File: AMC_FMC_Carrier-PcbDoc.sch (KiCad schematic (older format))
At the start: 17 parts

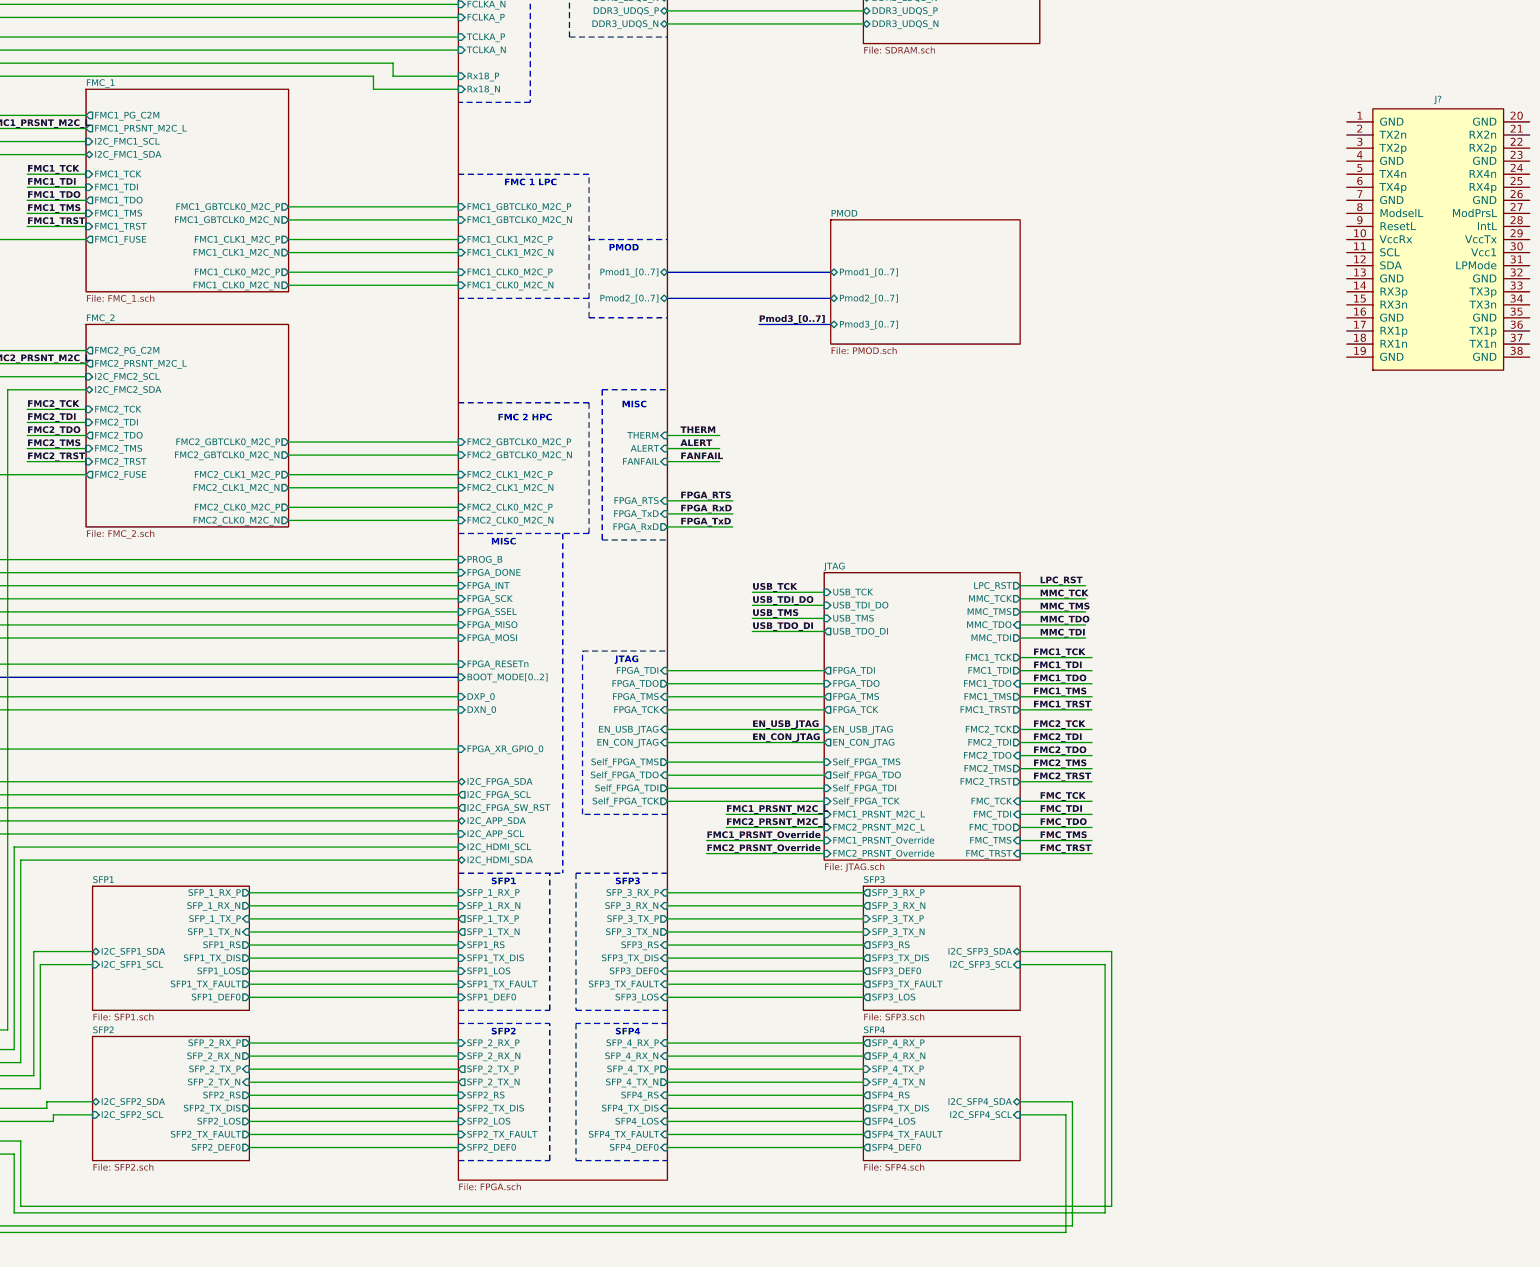
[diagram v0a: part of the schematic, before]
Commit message: MGT mux and QSFP added to the schematics,
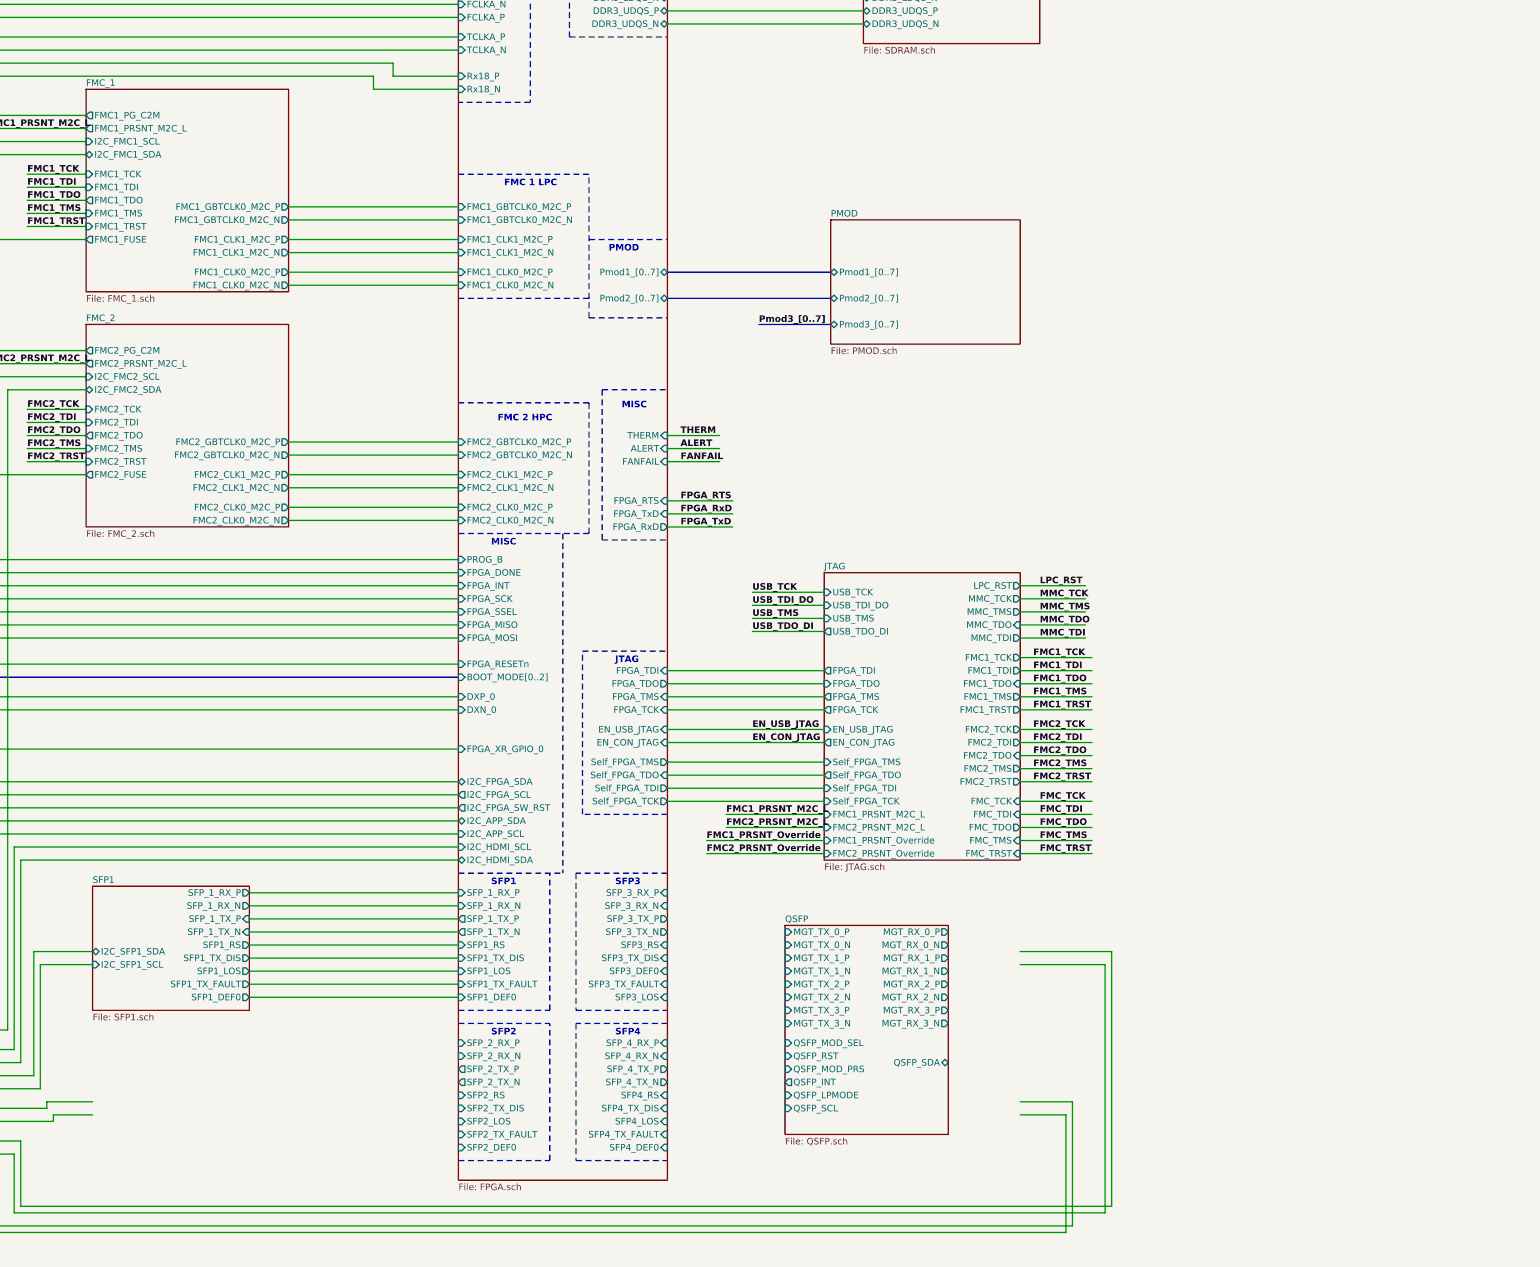
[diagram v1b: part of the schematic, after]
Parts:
- removed J?: SAMTEC_QSFP8-038-01-L-D-RA1, SAMTEC SMD:SAMTEC_QSFP8-038-01-L-D-RA1, symbol SAMTEC:SAMTEC_QSFP8-038-01-L-D-RA1
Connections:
- wire segments 364 -> 337
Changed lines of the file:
@@
 $Descr A2 23386 16535
 encoding utf-8
-Sheet 1 26
+Sheet 1 25
 Title "Marble"
 Date "2019-01-16"
@@
 Wire Wire Line
 	14450 5650 12950 5650
-$Sheet
-S 8550 13400 1200 950
-U 5CC393D3
-F0 "SFP2" 50
-F1 "SFP2.sch" 50
-F2 "SFP_2_RX_P" O R 9750 13450 50
-F3 "SFP_2_RX_N" O R 9750 13550 50
-F4 "SFP_2_TX_P" I R 9750 13650 50
-F5 "SFP_2_TX_N" I R 9750 13750 50
-F6 "I2C_SFP2_SDA" B L 8550 13900 50
-F7 "I2C_SFP2_SCL" I L 8550 14000 50
-F8 "SFP2_TX_DIS" O R 9750 13950 50
-F9 "SFP2_TX_FAULT" O R 9750 14150 50
-F10 "SFP2_DEF0" O R 9750 14250 50
-F11 "SFP2_LOS" O R 9750 14050 50
-F12 "SFP2_RS" O R 9750 13850 50
-$EndSheet
-$Sheet
-S 14450 12250 1200 950
-U 5CC6DBF7
-F0 "SFP3" 50
-F1 "SFP3.sch" 50
-F2 "SFP_3_RX_P" O L 14450 12300 50
-F3 "SFP_3_RX_N" O L 14450 12400 50
-F4 "SFP_3_TX_P" I L 14450 12500 50
-F5 "SFP_3_TX_N" I L 14450 12600 50
-F6 "I2C_SFP3_SDA" B R 15650 12750 50
-F7 "I2C_SFP3_SCL" I R 15650 12850 50
-F8 "SFP3_TX_DIS" O L 14450 12800 50
-F9 "SFP3_TX_FAULT" O L 14450 13000 50
-F10 "SFP3_DEF0" O L 14450 12900 50
-F11 "SFP3_LOS" O L 14450 13100 50
-F12 "SFP3_RS" O L 14450 12700 50
-$EndSheet
-$Sheet
-S 14450 13400 1200 950
-U 5CC8AFE1
-F0 "SFP4" 50
-F1 "SFP4.sch" 50
-F2 "SFP_4_RX_P" O L 14450 13450 50
-F3 "SFP_4_RX_N" O L 14450 13550 50
-F4 "SFP_4_TX_P" I L 14450 13650 50
-F5 "SFP_4_TX_N" I L 14450 13750 50
-F6 "I2C_SFP4_SDA" B R 15650 13900 50
-F7 "I2C_SFP4_SCL" I R 15650 14000 50
-F8 "SFP4_TX_DIS" O L 14450 13950 50
-F9 "SFP4_TX_FAULT" O L 14450 14150 50
-F10 "SFP4_DEF0" O L 14450 14250 50
-F11 "SFP4_LOS" O L 14450 14050 50
-F12 "SFP4_RS" O L 14450 13850 50
-$EndSheet
 Wire Wire Line
 	10050 7150 11350 7150
@@
 Text Notes 11700 6900 0    50   ~ 10
 FMC 1 LPC
-Wire Wire Line
-	14450 12300 12950 12300
-Wire Wire Line
-	14450 12400 12950 12400
-Wire Wire Line
-	14450 12500 12950 12500
-Wire Wire Line
-	14450 12600 12950 12600
-Wire Wire Line
-	14450 12800 12950 12800
-Wire Wire Line
-	14450 12900 12950 12900
-Wire Wire Line
-	14450 13000 12950 13000
-Wire Wire Line
-	14450 13100 12950 13100
-Wire Wire Line
-	14450 13450 12950 13450
-Wire Wire Line
-	14450 13550 12950 13550
-Wire Wire Line
-	14450 13650 12950 13650
-Wire Wire Line
-	14450 13750 12950 13750
-Wire Wire Line
-	14450 13950 12950 13950
-Wire Wire Line
-	14450 14050 12950 14050
-Wire Wire Line
-	14450 14150 12950 14150
-Wire Wire Line
-	14450 14250 12950 14250
 Wire Notes Line
 	11350 13200 12050 13200
@@
 	9750 13100 11350 13100
 Wire Wire Line
-	9750 13450 11350 13450
-Wire Wire Line
-	9750 13550 11350 13550
-Wire Wire Line
-	9750 13650 11350 13650
-Wire Wire Line
-	9750 13750 11350 13750
-Wire Wire Line
-	9750 13950 11350 13950
-Wire Wire Line
-	9750 14050 11350 14050
-Wire Wire Line
-	9750 14150 11350 14150
-Wire Wire Line
-	9750 14250 11350 14250
-Wire Wire Line
 	14450 3750 13700 3750
 Wire Wire Line
@@
 Wire Wire Line
 	9750 12700 11350 12700
-Wire Wire Line
-	9750 13850 11350 13850
-Wire Wire Line
-	12950 12700 14450 12700
-Wire Wire Line
-	12950 13850 14450 13850
 Wire Wire Line
 	10050 7050 11350 7050
@@
 Wire Wire Line
 	6800 6950 7450 6950
-$Comp
-L SAMTEC:SAMTEC_QSFP8-038-01-L-D-RA1 J?
-U 1 1 5E015188
-P 18350 6300
-F 0 "J?" H 18850 6373 50  0000 C CNN
-F 1 "SAMTEC_QSFP8-038-01-L-D-RA1" H 18350 4225 50  0001 L CNN
-F 2 "SAMTEC SMD:SAMTEC_QSFP8-038-01-L-D-RA1" H 18350 4150 50  0001 L CNN
-F 3 " " H 18350 4075 50  0001 L CNN
-F 4 "QSFP+" H 18350 3100 50  0001 L CNN "Family"
-F 5 "SAMTEC_QSFP8-038-01-L-D-RA1" H 18350 4000 50  0001 L CNN "Part Number"
-F 6 "QSFP+x1" H 18350 3925 50  0001 L CNN "Library Ref"
-F 7 "SchLib\\Connectors.SchLib" H 18350 3850 50  0001 L CNN "Library Path"
-F 8 " " H 18350 3775 50  0001 L CNN "Comment"
-F 9 "Standard" H 18350 3700 50  0001 L CNN "Component Kind"
-F 10 "Standard" H 18350 3625 50  0001 L CNN "Component Type"
-F 11 " " H 18350 3550 50  0001 L CNN "Device"
-F 12 " " H 18350 3475 50  0001 L CNN "PackageDescription"
-F 13 "38" H 18350 3400 50  0001 L CNN "Pin Count"
-F 14 " " H 18350 3325 50  0001 L CNN "Case"
-F 15 "PcbLib\\SAMTEC SMD.PcbLib" H 18350 3250 50  0001 L CNN "Footprint Path"
-F 16 "SAMTEC_QSFP8-038-01-L-D-RA1" H 18350 3175 50  0001 L CNN "Footprint Ref"
-F 17 "Yes" H 18350 3025 50  0001 L CNN "Mounted"
-F 18 "No" H 18350 2950 50  0001 L CNN "Socket"
-F 19 "No" H 18350 2875 50  0001 L CNN "PressFit"
-F 20 "No" H 18350 2800 50  0001 L CNN "Sense"
-F 21 " " H 18350 2725 50  0001 L CNN "Sense Comment"
-F 22 "Yes" H 18350 2650 50  0001 L CNN "SMD"
-F 23 " " H 18350 2575 50  0001 L CNN "Status Comment"
-F 24 "None" H 18350 2500 50  0001 L CNN "Status"
-F 25 " " H 18350 2425 50  0001 L CNN "SCEM"
-F 26 "Dual Row 38 positions, Pitch 0.8mm, QSFP+ Right Angle Edge Connector" H 18350 2350 50  0001 L CNN "Part Description"
-F 27 "SAMTEC" H 18350 2275 50  0001 L CNN "Manufacturer"
-F 28 "QSFP8-038-01-L-D-RA1" H 18350 2200 50  0001 L CNN "Manufacturer Part Number"
-F 29 "5.35mm" H 18350 2125 50  0001 L CNN "ComponentHeight"
-F 30 " " H 18350 2050 50  0001 L CNN "ComponentLink1Description"
-F 31 " " H 18350 1975 50  0001 L CNN "ComponentLink2Description"
-F 32 "CERN DEM JLC" H 18350 1900 50  0001 L CNN "Author"
-F 33 "08/14/13 00:00:00" H 18350 1825 50  0001 L CNN "CreateDate"
-F 34 "08/14/13 00:00:00" H 18350 1750 50  0001 L CNN "LatestRevisionDate"
-F 35 "SAMTEC" H 18350 1675 50  0001 L CNN "Database Table Name"
-F 36 "Connectors.DbLib" H 18350 1600 50  0001 L CNN "Library Name"
-F 37 "SAMTEC SMD" H 18350 1525 50  0001 L CNN "Footprint Library"
-F 38 "This work is licensed under the Creative Commons CC-BY-SA 4.0 License. To the extent that circuit schematics that use Licensed Material can be considered to be ‘Adapted Material’, then the copyright holder waives article 3.b of the license with respect to these schematics." H 18350 1450 50  0001 L CNN "License"
-	1    18350 6300
-	1    0    0    -1
-$EndComp
+$Sheet
+S 13850 12550 1250 1600
+U 5E7FBE93
+F0 "QSFP" 50
+F1 "QSFP.sch" 50
+F2 "QSFP_MOD_SEL" I L 13850 13450 50
+F3 "QSFP_RST" I L 13850 13550 50
+F4 "QSFP_MOD_PRS" I L 13850 13650 50
+F5 "QSFP_INT" O L 13850 13750 50
+F6 "QSFP_LPMODE" I L 13850 13850 50
+F7 "QSFP_SCL" I L 13850 13950 50
+F8 "QSFP_SDA" B R 15100 13600 50
+F9 "MGT_TX_0_P" I L 13850 12600 50
+F10 "MGT_TX_0_N" I L 13850 12700 50
+F11 "MGT_TX_1_P" I L 13850 12800 50
+F12 "MGT_TX_1_N" I L 13850 12900 50
+F13 "MGT_TX_2_P" I L 13850 13000 50
+F14 "MGT_TX_2_N" I L 13850 13100 50
+F15 "MGT_TX_3_P" I L 13850 13200 50
+F16 "MGT_TX_3_N" I L 13850 13300 50
+F17 "MGT_RX_0_P" O R 15100 12600 50
+F18 "MGT_RX_0_N" O R 15100 12700 50
+F19 "MGT_RX_1_P" O R 15100 12800 50
+F20 "MGT_RX_1_N" O R 15100 12900 50
+F21 "MGT_RX_2_P" O R 15100 13000 50
+F22 "MGT_RX_2_N" O R 15100 13100 50
+F23 "MGT_RX_3_P" O R 15100 13200 50
+F24 "MGT_RX_3_N" O R 15100 13300 50
+$EndSheet
 $EndSCHEMATC

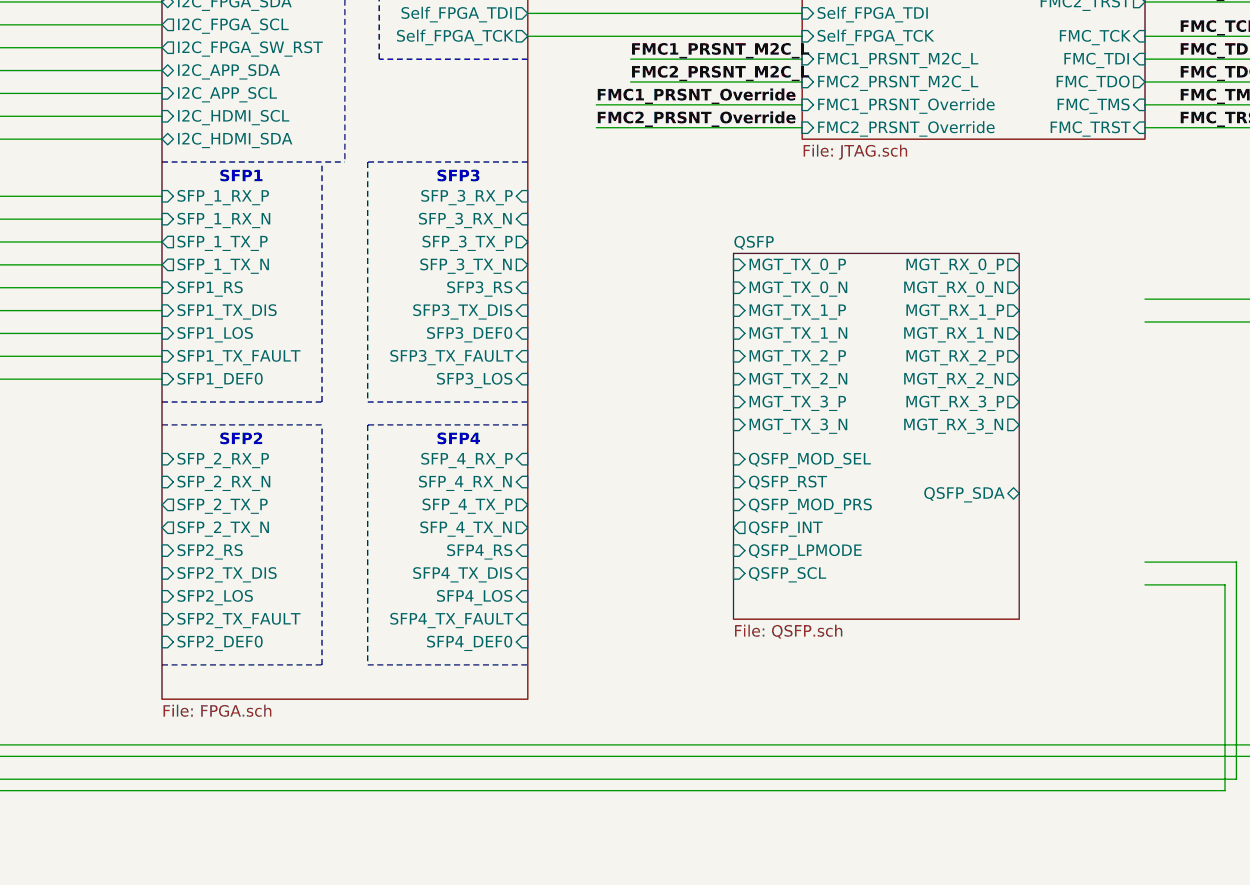
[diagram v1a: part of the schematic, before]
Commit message: FMC HPC & LPC done, FPGA power delivery done, RGMII lines done,  MGT lines progress
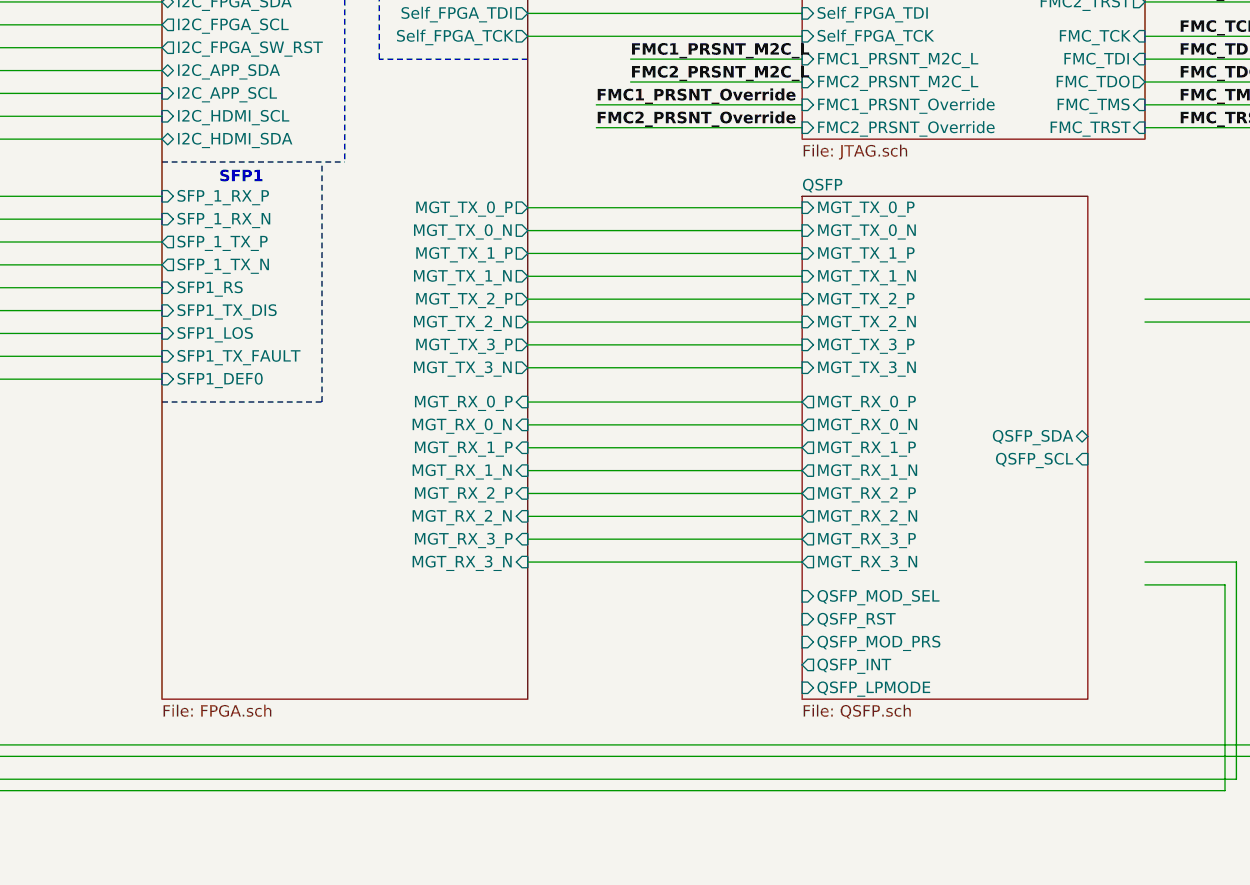
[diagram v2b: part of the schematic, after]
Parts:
- HS1: value HSINK_ATS_ATS-50350B-C1-R0 -> HS_AAVID_342947; footprint Heat-Sinks:HSINK_ATS_ATS-50350B-C1-R0 -> po konwersji:HS_AAVID_342947; Footprint Ref HSINK_ATS_ATS-50350B-C1-R0 -> HS_AAVID_342947; Manufacturer Part Number ATS-50350B-C1-R0 -> HS_AAVID_342947; Part Number HSINK_ATS_ATS-50350B-C1-R0 -> HS_AAVID_342947
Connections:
- wire segments 337 -> 353
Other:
- note removed: "SFP2"
- note removed: "SFP3"
- note removed: "SFP4"
